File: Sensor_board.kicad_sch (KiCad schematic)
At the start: 16 parts, among them J1 Mic_Conn, U1 TLV741PxxDBVx

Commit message: Big commit for the day
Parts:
- renumbered C10 to C?, C11 to C?, CB1 to CB?, CB3 to CB?
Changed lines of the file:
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@@
   (symbol (lib_id "Device:C_Small") (at 81.28 137.16 0) (unit 1)
     (in_bom yes) (on_board yes) (dnp no)
-    (property "Reference" "CB1" (at 83.6168 135.9916 0)
+    (property "Reference" "CB?" (at 83.6168 135.9916 0)
       (effects (font (size 1.27 1.27)) (justify left))
     )
@@
   (symbol (lib_id "power:GND") (at 81.28 139.7 0) (unit 1)
     (in_bom yes) (on_board yes) (dnp no)
-    (property "Reference" "#PWR02" (at 81.28 146.05 0)
+    (property "Reference" "#PWR?" (at 81.28 146.05 0)
       (effects (font (size 1.27 1.27)) hide)
     )
@@
   (symbol (lib_id "Device:C_Small") (at 176.53 72.39 0) (unit 1)
     (in_bom yes) (on_board yes) (dnp no)
-    (property "Reference" "CB3" (at 178.8668 71.2216 0)
+    (property "Reference" "CB?" (at 178.8668 71.2216 0)
       (effects (font (size 1.27 1.27)) (justify left))
     )
@@
   (symbol (lib_id "Device:C_Small") (at 138.43 57.15 270) (unit 1)
     (in_bom yes) (on_board yes) (dnp no)
-    (property "Reference" "C10" (at 138.43 51.3334 90)
+    (property "Reference" "C?" (at 138.43 51.3334 90)
       (effects (font (size 1.27 1.27)))
     )
@@
   (symbol (lib_id "Device:C_Small") (at 138.43 62.23 270) (unit 1)
     (in_bom yes) (on_board yes) (dnp no)
-    (property "Reference" "C11" (at 135.89 64.77 90)
-      (effects (font (size 1.27 1.27)))
-    )
+    (property "Reference" "C?" (at 135.89 64.77 90)
+      (effects (font (size 1.27 1.27)))
+    )

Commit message: (bc) large commit with spice experiments
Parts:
- gave numbers to parts that had none: 4

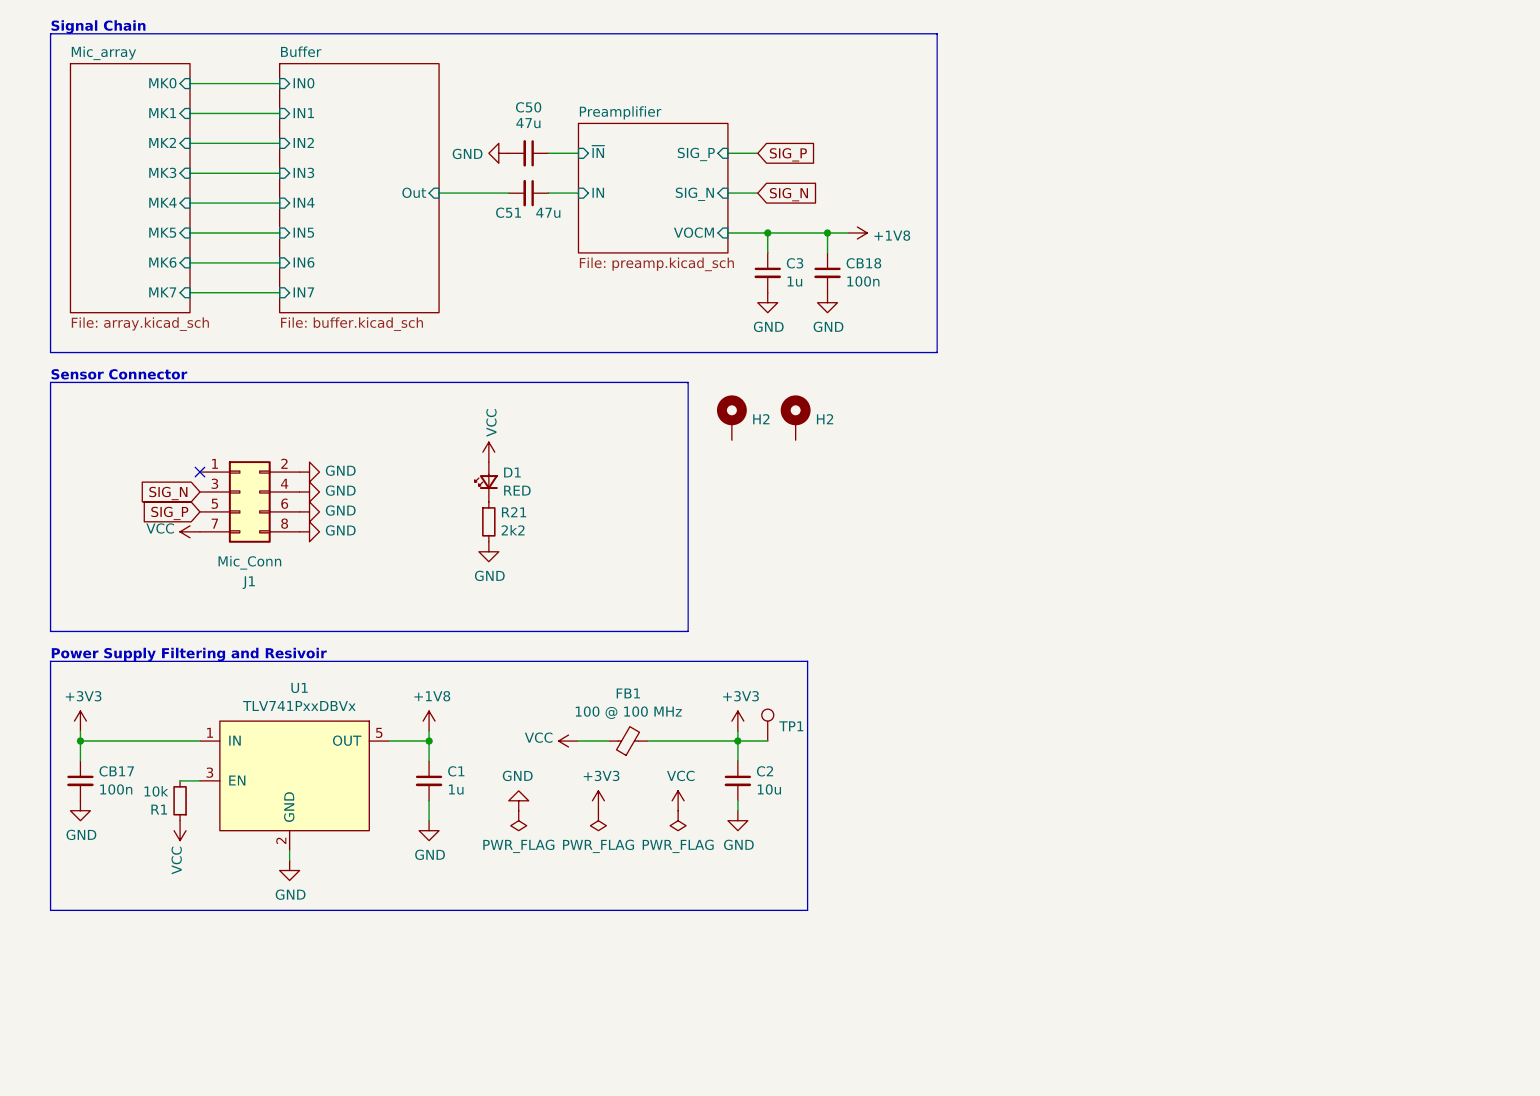
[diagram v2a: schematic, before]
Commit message: (bc) new summation preamp & seperate power net
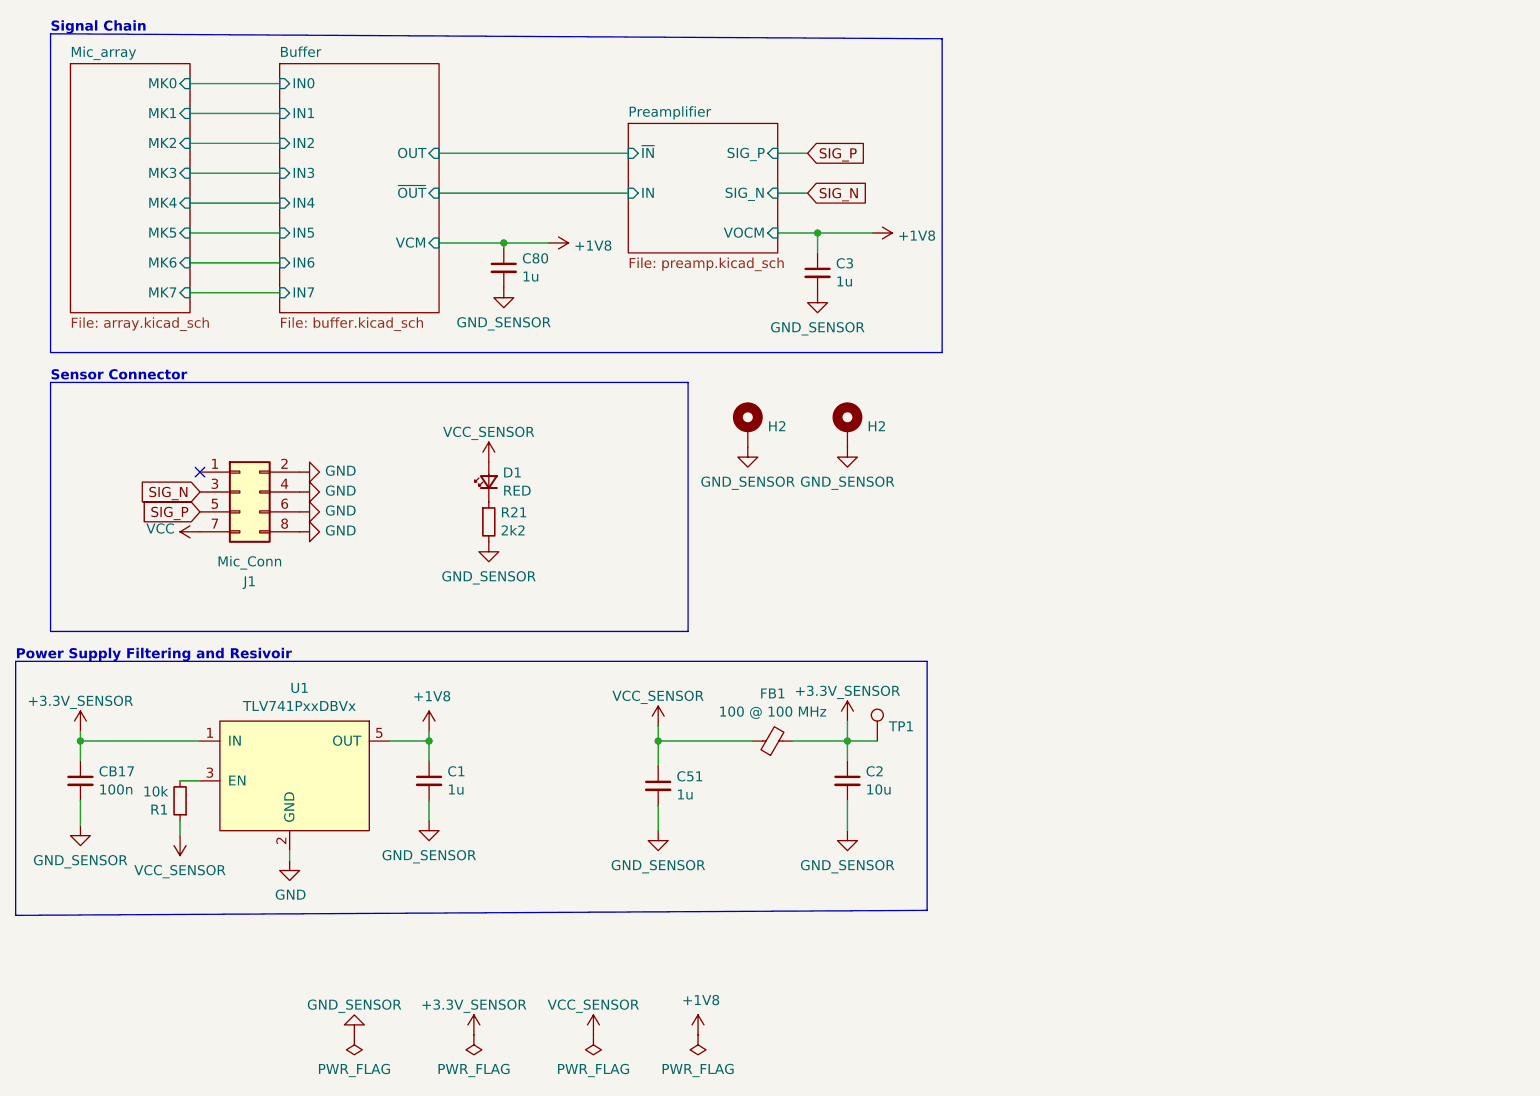
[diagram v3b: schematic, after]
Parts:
- removed C50: 47u, Capacitor_SMD:C_1206_3216Metric_Pad1.33x1.80mm_HandSolder, symbol Device:C_Small
- removed CB18: 100n, Capacitor_SMD:C_0603_1608Metric_Pad1.08x0.95mm_HandSolder, symbol Device:C_Small
- added C80: 1u, Capacitor_SMD:C_0603_1608Metric_Pad1.08x0.95mm_HandSolder, symbol Device:C_Small
- C51: value 47u -> 1u; footprint Capacitor_SMD:C_1206_3216Metric_Pad1.33x1.80mm_HandSolder -> Capacitor_SMD:C_0603_1608Metric_Pad1.08x0.95mm_HandSolder; MPN GRM31CR60J107KE39K -> C0603C105K8RACTU; Mfr. Murata Electronics -> KEMET; Notes Specified 47u but that is min. (>47u is better) -> (none)
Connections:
- net Buffer/Out is gone; now on net GND: C51.2
- net Preamplifier/IN is gone; now on net +3.3V: C51.1
- net +1V8: now also C80.1
- net GND: now also H2.1, H2.1, C80.2
- net VCC: no longer D1.2 (A), FB1.1, R1.1
- net +3V3 renamed +3.3V
- net +3.3V: now also D1.2 (A), FB1.1, R1.1
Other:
- sheet Buffer ports: added OUT, VCM, ~{OUT}; removed Out
- moved on the sheet: C2, C3, FB1, H2, TP1

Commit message: (sch) relabel
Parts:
- renumbered C1 to C1001, C80 to C1002, C51 to C1003, C3 to C1004, C2 to C1005, CB17 to CB1001, D1 to D1001, FB1 to FB1001, J1 to J1001, R1 to R1001, R21 to R1002, TP1 to TP1001, U1 to U1001

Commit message: (bc) finish up ERC
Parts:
- removed FB1001: 100 @ 100 MHz, Inductor_SMD:L_0603_1608Metric_Pad1.05x0.95mm_HandSolder, symbol Sensor_Board-rescue:Ferrite_Bead_Small-Device
- removed J1001: Mic_Conn, grootvoet:TE_7-215079-8, symbol Connector_Generic:Conn_02x04_Odd_Even
- added FB904: 100@100MHz, Inductor_SMD:L_0603_1608Metric_Pad1.05x0.95mm_HandSolder, symbol Device:FerriteBead_Small
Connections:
- net +3.3V: now also FB904.1, FB904.2
- no-connect marks 1 -> 0
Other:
- added sheet Sensor_Conn_3 (Sensor_Connector.kicad_sch)
- note removed: "Sensor Connector"
- moved on the sheet: C1001, C1003, C1005, CB1001, D1001, H2, R1001, R1002, TP1001, U1001

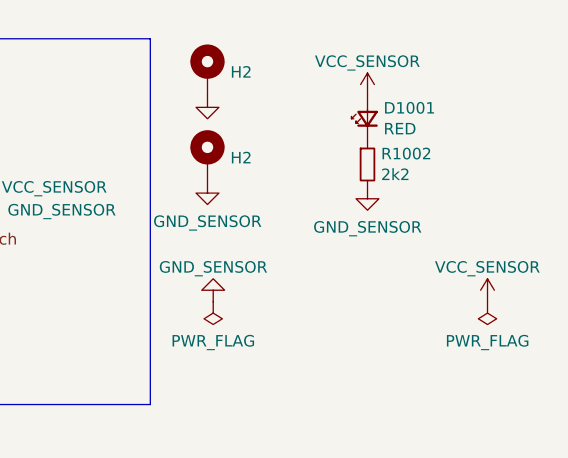
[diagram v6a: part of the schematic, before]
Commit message: (sch) change passives to 0402
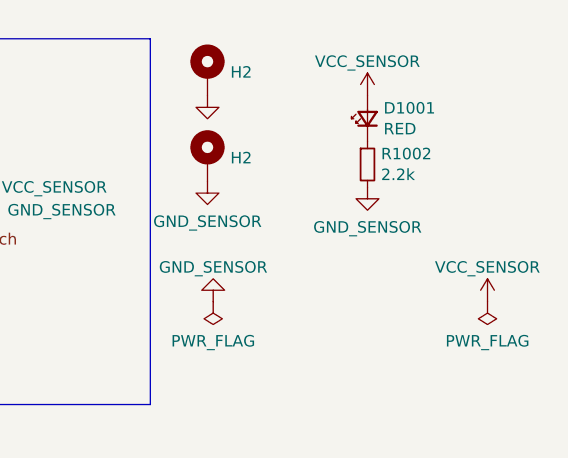
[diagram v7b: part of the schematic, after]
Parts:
- D1001: footprint LED_SMD:LED_0603_1608Metric_Pad1.05x0.95mm_HandSolder -> LED_SMD:LED_0603_1608Metric
- R1001: footprint Resistor_SMD:R_0603_1608Metric_Pad0.98x0.95mm_HandSolder -> Resistor_SMD:R_0402_1005Metric; MPN RC0603JR-0710KL -> RT0402FRE1310KL
- R1002: value 2k2 -> 2.2k; footprint Resistor_SMD:R_0603_1608Metric_Pad0.98x0.95mm_HandSolder -> Resistor_SMD:R_0402_1005Metric; MPN ERJ-3EKF2201V -> RT0402FRE072K2L; Mfr. Panasonic -> Yageo
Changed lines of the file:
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@@
       (effects (font (size 1.27 1.27)) (justify right))
     )
-    (property "Footprint" "LED_SMD:LED_0603_1608Metric_Pad1.05x0.95mm_HandSolder" (at 245.11 50.8 90)
+    (property "Footprint" "LED_SMD:LED_0603_1608Metric" (at 245.11 50.8 90)
       (effects (font (size 1.27 1.27)) hide)
     )
@@
       (effects (font (size 1.27 1.27)) (justify left))
     )
-    (property "Value" "2k2" (at 246.6086 57.023 0)
+    (property "Value" "2.2k" (at 246.6086 57.023 0)
       (effects (font (size 1.27 1.27)) (justify left))
     )
-    (property "Footprint" "Resistor_SMD:R_0603_1608Metric_Pad0.98x0.95mm_HandSolder" (at 245.11 55.88 0)
+    (property "Footprint" "Resistor_SMD:R_0402_1005Metric" (at 245.11 55.88 0)
       (effects (font (size 1.27 1.27)) hide)
     )
@@
       (effects (font (size 1.27 1.27)) hide)
     )
-    (property "MPN" "ERJ-3EKF2201V" (at 245.11 55.88 0)
+    (property "MPN" "RT0402FRE072K2L" (at 245.11 55.88 0)
       (effects (font (size 1.27 1.27)) hide)
     )
-    (property "Mfr." "Panasonic" (at 245.11 55.88 0)
+    (property "Mfr." "Yageo" (at 245.11 55.88 0)
       (effects (font (size 1.27 1.27)) hide)
     )
@@
       (effects (font (size 1.27 1.27)) (justify left))
     )
-    (property "Footprint" "Resistor_SMD:R_0603_1608Metric_Pad0.98x0.95mm_HandSolder" (at 99.06 104.775 0)
+    (property "Footprint" "Resistor_SMD:R_0402_1005Metric" (at 99.06 104.775 0)
       (effects (font (size 1.27 1.27)) hide)
     )
@@
       (effects (font (size 1.27 1.27)) hide)
     )
-    (property "MPN" "RC0603JR-0710KL" (at 99.06 104.775 0)
+    (property "MPN" "RT0402FRE1310KL" (at 99.06 104.775 0)
       (effects (font (size 1.27 1.27)) hide)
     )

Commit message: (pcb) initial layout
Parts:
- CB1001: footprint Capacitor_SMD:C_0603_1608Metric_Pad1.08x0.95mm_HandSolder -> Capacitor_SMD:C_0402_1005Metric; MPN C0603C104M5RACTU -> C0402C104K8PACTU
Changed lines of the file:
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@@
       (effects (font (size 1.27 1.27)) (justify left))
     )
-    (property "Footprint" "Capacitor_SMD:C_0603_1608Metric_Pad1.08x0.95mm_HandSolder" (at 86.36 102.235 0)
+    (property "Footprint" "Capacitor_SMD:C_0402_1005Metric" (at 86.36 102.235 0)
       (effects (font (size 1.27 1.27)) hide)
     )
@@
       (effects (font (size 1.27 1.27)) hide)
     )
-    (property "MPN" "C0603C104M5RACTU" (at 86.36 102.235 0)
+    (property "MPN" "C0402C104K8PACTU" (at 86.36 102.235 0)
       (effects (font (size 1.27 1.27)) hide)
     )
